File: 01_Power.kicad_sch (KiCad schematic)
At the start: 24 parts, among them Q1 SI3421DV, Q2 SI3421DV, U1 CYPD3177_24x

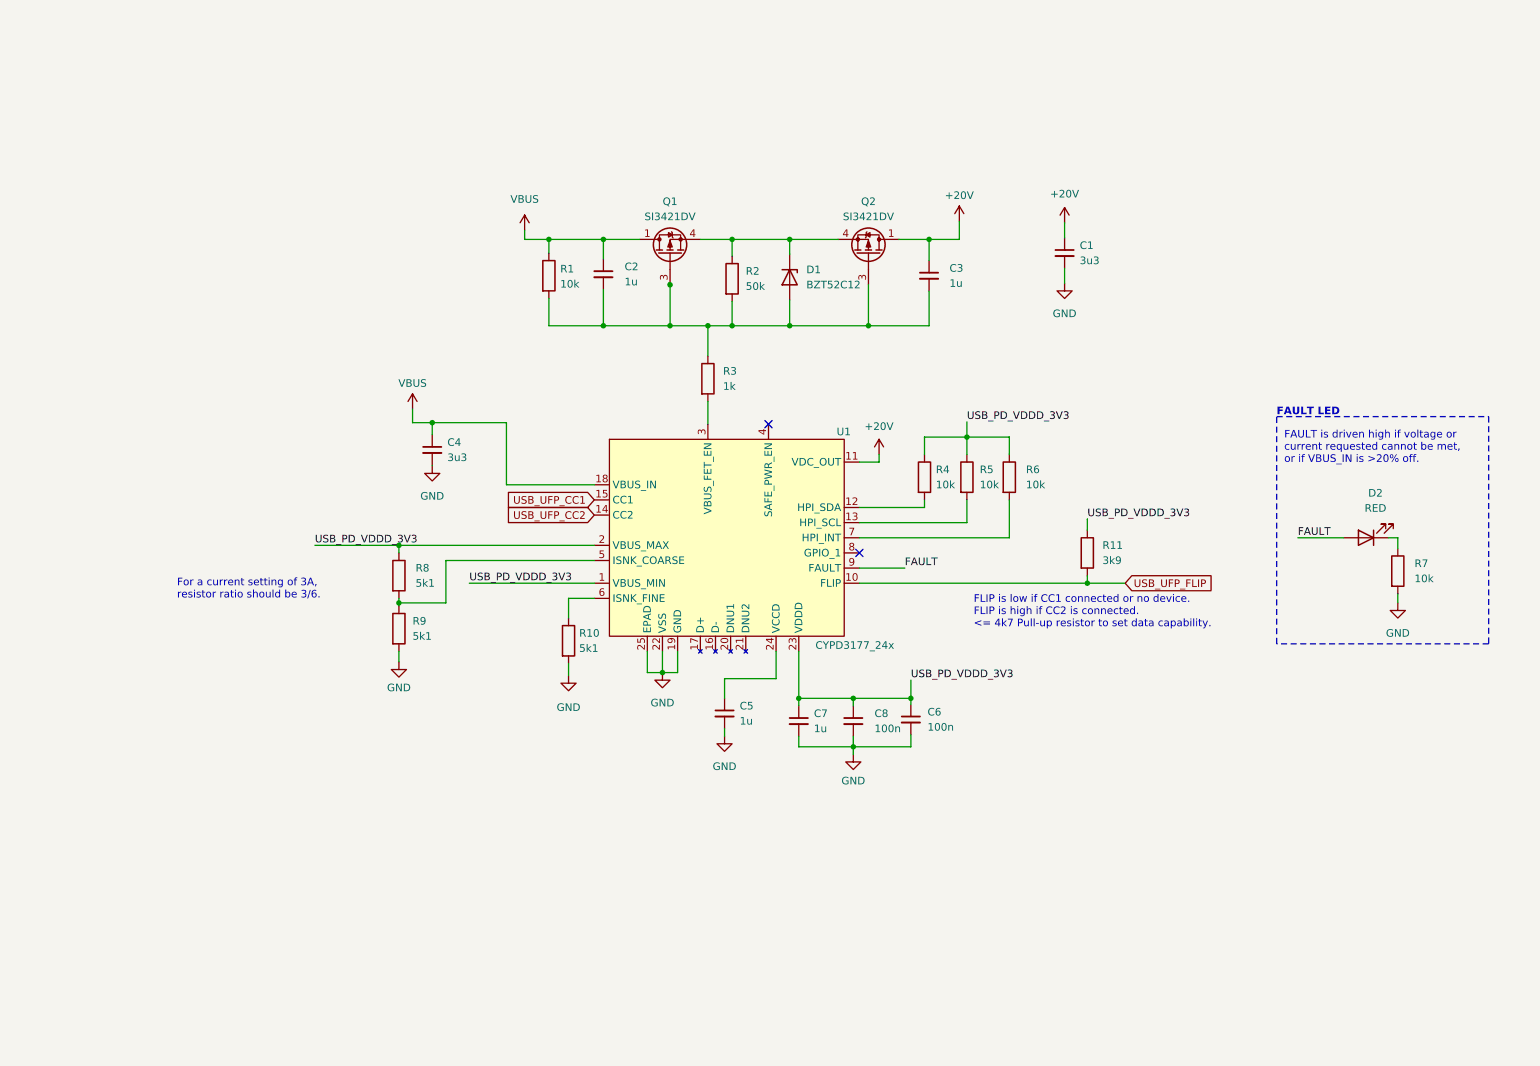
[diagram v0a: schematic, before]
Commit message: Add ESD protection for UFP, create buck converter model
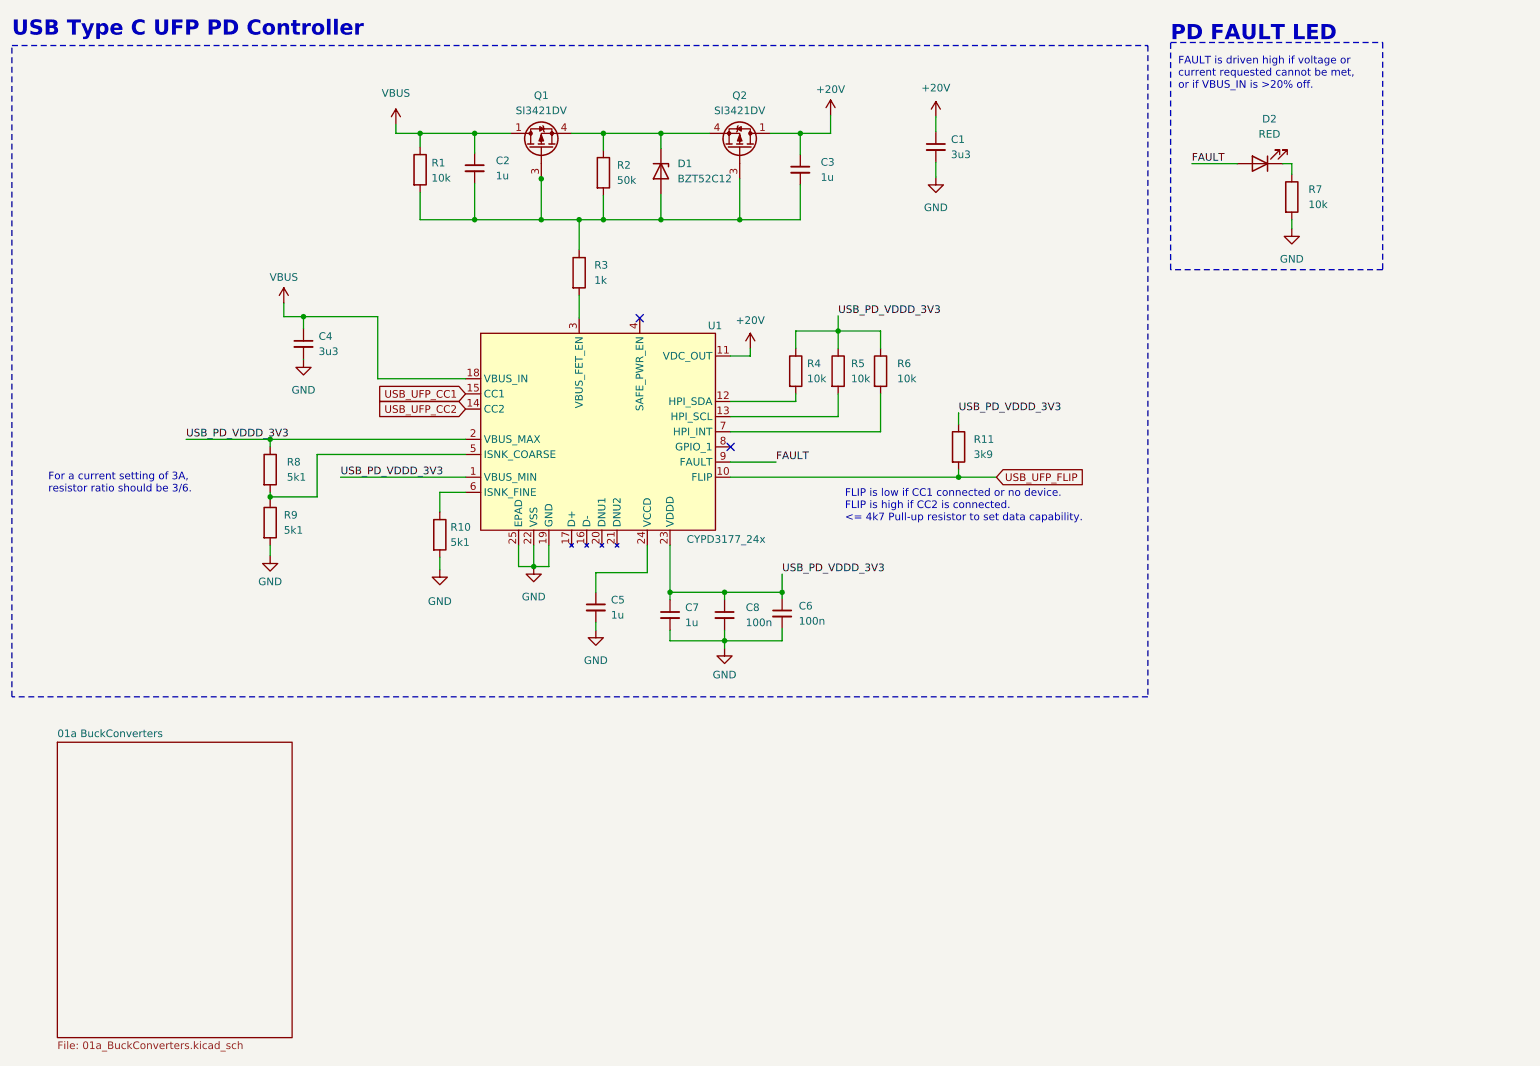
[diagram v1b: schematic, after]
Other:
- added sheet 01a BuckConverters (01a_BuckConverters.kicad_sch)
- note added: "PD FAULT LED"
- note added: "USB Type C UFP PD Controller"
- note removed: "FAULT LED"
- moved on the sheet: C1, C2, C3, C4, C5, C6, C7, C8, D1, D2, Q1, Q2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

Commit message: more work on the power section
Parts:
- C1: value 3u3 -> 100u
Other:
- sheet 01a BuckConverters renamed 01a VoltageRegulators
- added sheet 01b VoltageRegulators (01b_VoltageRegulators.kicad_sch)
- sheet 01a VoltageRegulators: file 01a_BuckConverters.kicad_sch -> 01a_VoltageRegulators.kicad_sch
- moved on the sheet: C1, C2, C3, C4, C5, C6, C7, C8, D1, D2, Q1, Q2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

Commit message: add usb hub controller schematic, fix up redriver
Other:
- removed sheet 01b VoltageRegulators
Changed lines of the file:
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@@
-    )
-  )
-  (sheet (at 67.31 137.16) (size 43.18 49.53) (fields_autoplaced)
-    (stroke (width 0.1524) (type solid))
-    (fill (color 0 0 0 0.0000))
-    (property "Sheetname" "01b VoltageRegulators" (at 67.31 136.4484 0)
-      (effects (font (size 1.27 1.27)) (justify left bottom))
-    )
-    (property "Sheetfile" "01b_VoltageRegulators.kicad_sch" (at 67.31 187.2746 0)
-      (effects (font (size 1.27 1.27)) (justify left top))
-    )
-    (instances
-      (project "USBHUB"
-        (path "/d5edc647-9ac3-4ac1-ab8a-57c77be3f4d3/2bd96af5-5a66-4797-badd-32cacbbf4fbd" (page "7"))
-      )
     )
   )

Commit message: finish up schematics and ERC
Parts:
- Q1, Q2: symbol catSink:SI3421DV -> CakeUSB:SI3421DV
- U1: symbol Cake_USB:CYPD3177_24x -> CakeUSB:CYPD3177_24x
- renumbered R9 to R10, R10 to R11, R7 to R3, R3 to R4, R4 to R5, R5 to R6, R6 to R7, R11 to R8, R8 to R9

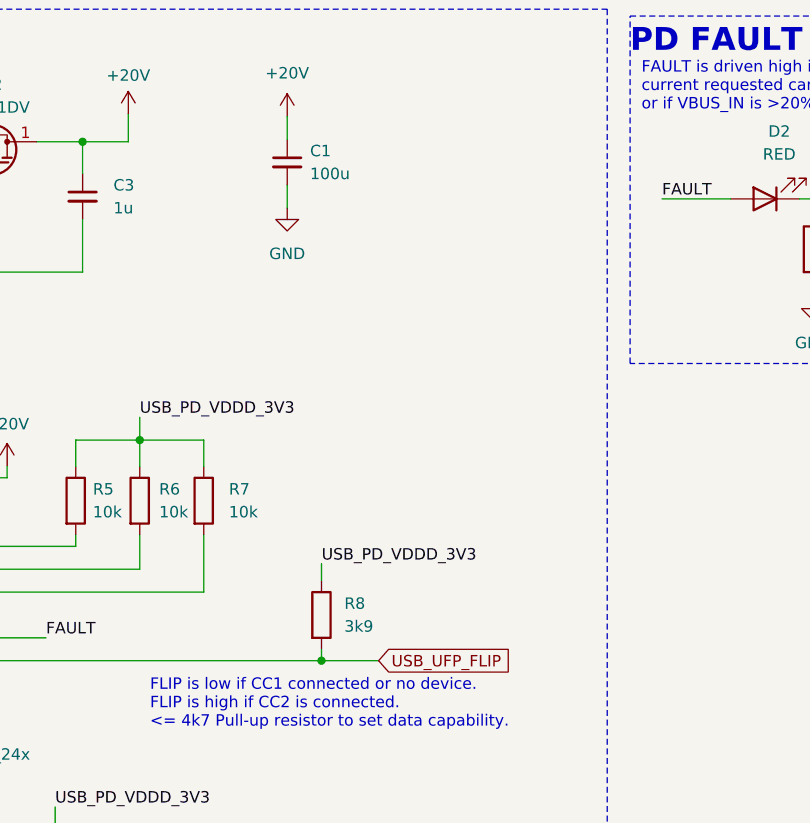
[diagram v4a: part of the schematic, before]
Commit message: finish setting footprints
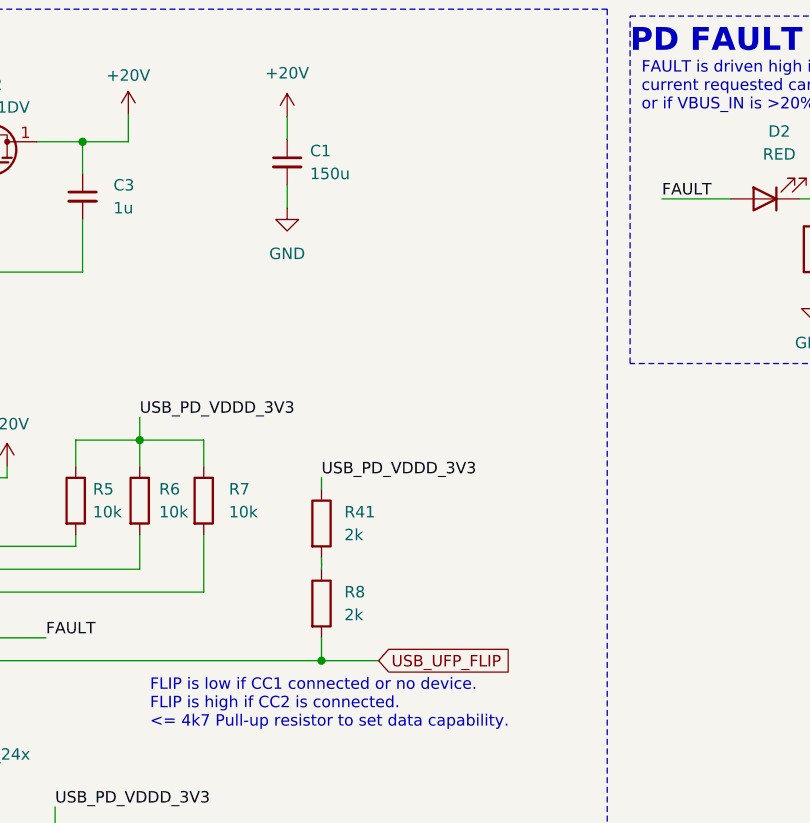
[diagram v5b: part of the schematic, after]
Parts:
- added R41: 2k, Resistor_SMD:R_0402_1005Metric, symbol Device:R
- C1: value 100u -> 150u; footprint Capacitor_SMD:C_0603_1608Metric -> Capacitor_SMD:C_Elec_6.3x7.7
- R8: value 3k9 -> 2k; footprint (none) -> Resistor_SMD:R_0402_1005Metric
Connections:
- net USB_PD_VDDD_3V3: now also R41.1; no longer R8.1
- new net: R41.2, R8.1
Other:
- moved on the sheet: R8
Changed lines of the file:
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@@
+    (stroke (width 0) (type default))
+  )
+  (wire (pts (xy 173.99 76.8879) (xy 173.99 76.2))
     (stroke (width 0) (type default))
   )
@@
     (stroke (width 0) (type default))
   )
-  (wire (pts (xy 173.99 86.36) (xy 173.99 87.63))
+  (wire (pts (xy 173.99 85.09) (xy 173.99 87.63))
     (stroke (width 0) (type default))
   )
@@
     (stroke (width 0) (type default))
   )
-  (wire (pts (xy 173.99 78.74) (xy 173.99 76.8879))
+  (wire (pts (xy 173.99 77.47) (xy 174.0084 76.8879))
     (stroke (width 0) (type default))
   )
@@
     (stroke (width 0) (type default))
   )
+  (wire (pts (xy 173.99 76.8879) (xy 174.0084 76.8879))
+    (stroke (width 0) (type default))
+  )
   (wire (pts (xy 153.797 63.119) (xy 153.797 66.04))
     (stroke (width 0) (type default))
@@
     (stroke (width 0) (type default))
   )
+  (wire (pts (xy 173.99 67.31) (xy 173.99 68.58))
+    (stroke (width 0) (type default))
+  )
   (wire (pts (xy 170.18 34.798) (xy 170.18 37.338))
     (stroke (width 0) (type default))
@@
   )
   (wire (pts (xy 125.603 106.934) (xy 125.603 108.204))
-    (stroke (width 0) (type default))
-  )
-  (wire (pts (xy 173.99 76.8879) (xy 174.0084 76.8879))
     (stroke (width 0) (type default))
   )
@@
     (effects (font (size 1.27 1.27)) (justify left bottom))
   )
-  (label "USB_PD_VDDD_3V3" (at 174.0084 76.8879 0) (fields_autoplaced)
+  (label "USB_PD_VDDD_3V3" (at 173.99 67.31 0) (fields_autoplaced)
     (effects (font (size 1.27 1.27)) (justify left bottom))
   )
@@
       (effects (font (size 1.27 1.27)) (justify left))
     )
-    (property "Value" "100u" (at 172.72 33.5343 0)
-      (effects (font (size 1.27 1.27)) (justify left))
-    )
-    (property "Footprint" "Capacitor_SMD:C_0603_1608Metric" (at 170.18 32.258 0)
+    (property "Value" "150u" (at 172.72 33.5343 0)
+      (effects (font (size 1.27 1.27)) (justify left))
+    )
+    (property "Footprint" "Capacitor_SMD:C_Elec_6.3x7.7" (at 170.18 32.258 0)
       (effects (font (size 1.27 1.27)) hide)
     )
@@
     )
   )
-  (symbol (lib_id "Device:R") (at 173.99 82.55 0) (unit 1)
-    (in_bom yes) (on_board yes) (dnp no) (fields_autoplaced)
-    (property "Reference" "R8" (at 176.53 81.28 0)
-      (effects (font (size 1.27 1.27)) (justify left))
-    )
-    (property "Value" "3k9" (at 176.53 83.82 0)
-      (effects (font (size 1.27 1.27)) (justify left))
-    )
-    (property "Footprint" "" (at 172.212 82.55 90)
-      (effects (font (size 1.27 1.27)) hide)
-    )
-    (property "Datasheet" "~" (at 173.99 82.55 0)
+  (symbol (lib_id "Device:R") (at 173.99 81.28 0) (unit 1)
+    (in_bom yes) (on_board yes) (dnp no) (fields_autoplaced)
+    (property "Reference" "R8" (at 176.53 80.01 0)
+      (effects (font (size 1.27 1.27)) (justify left))
+    )
+    (property "Value" "2k" (at 176.53 82.55 0)
+      (effects (font (size 1.27 1.27)) (justify left))
+    )
+    (property "Footprint" "Resistor_SMD:R_0402_1005Metric" (at 172.212 81.28 90)
+      (effects (font (size 1.27 1.27)) hide)
+    )
+    (property "Datasheet" "~" (at 173.99 81.28 0)
       (effects (font (size 1.27 1.27)) hide)
     )
@@
         )
       )
+    )
+  )
+  (symbol (lib_id "Device:R") (at 173.99 72.39 0) (unit 1)
+    (in_bom yes) (on_board yes) (dnp no) (fields_autoplaced)
+    (property "Reference" "R41" (at 176.53 71.12 0)
+      (effects (font (size 1.27 1.27)) (justify left))
+    )
+    (property "Value" "2k" (at 176.53 73.66 0)
+      (effects (font (size 1.27 1.27)) (justify left))
+    )
+    (property "Footprint" "Resistor_SMD:R_0402_1005Metric" (at 172.212 72.39 90)
+      (effects (font (size 1.27 1.27)) hide)
+    )
+    (property "Datasheet" "~" (at 173.99 72.39 0)
+      (effects (font (size 1.27 1.27)) hide)
+    )
+    (pin "2")
+    (pin "1")
+    (instances
+      (project "USBHUB"
+        (path "/d5edc647-9ac3-4ac1-ab8a-57c77be3f4d3/2bd96af5-5a66-4797-badd-32cacbbf4fbd"
+          (reference "R41") (unit 1)
+        )
+      )

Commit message: symbol fixes, switch ESD protection for USB datalines
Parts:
- U1: footprint Cake_USB:CYPD3177_24LQx_QFN-24_EP_4x4_Pitch0.5mm -> CakeUSB:CYPD3177_24LQx_QFN-24_EP_4x4_Pitch0.5mm
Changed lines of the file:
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@@
       (effects (font (size 1.27 1.27)) (justify left))
     )
-    (property "Footprint" "Cake_USB:CYPD3177_24LQx_QFN-24_EP_4x4_Pitch0.5mm" (at 161.163 46.99 0)
+    (property "Footprint" "CakeUSB:CYPD3177_24LQx_QFN-24_EP_4x4_Pitch0.5mm" (at 161.163 46.99 0)
       (effects (font (size 1.27 1.27)) hide)
     )

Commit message: fix symbols, route UFP DPs and voltage regs
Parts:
- R1, R3, R5, R6, R7: footprint Resistor_SMD:R_0603_1608Metric -> Resistor_SMD:R_0402_1005Metric
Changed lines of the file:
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@@
       (effects (font (size 1.27 1.27)) (justify left))
     )
-    (property "Footprint" "Resistor_SMD:R_0603_1608Metric" (at 152.019 69.85 90)
+    (property "Footprint" "Resistor_SMD:R_0402_1005Metric" (at 152.019 69.85 90)
       (effects (font (size 1.27 1.27)) hide)
     )
@@
       (effects (font (size 1.27 1.27)) (justify left))
     )
-    (property "Footprint" "Resistor_SMD:R_0603_1608Metric" (at 159.131 69.85 90)
+    (property "Footprint" "Resistor_SMD:R_0402_1005Metric" (at 159.131 69.85 90)
       (effects (font (size 1.27 1.27)) hide)
     )
@@
       (effects (font (size 1.27 1.27)) (justify left))
     )
-    (property "Footprint" "Resistor_SMD:R_0603_1608Metric" (at 81.915 36.068 90)
+    (property "Footprint" "Resistor_SMD:R_0402_1005Metric" (at 81.915 36.068 90)
       (effects (font (size 1.27 1.27)) hide)
     )
@@
       (effects (font (size 1.27 1.27)) (justify left))
     )
-    (property "Footprint" "Resistor_SMD:R_0603_1608Metric" (at 226.822 41.91 90)
+    (property "Footprint" "Resistor_SMD:R_0402_1005Metric" (at 226.822 41.91 90)
       (effects (font (size 1.27 1.27)) hide)
     )
@@
       (effects (font (size 1.27 1.27)) (justify left))
     )
-    (property "Footprint" "Resistor_SMD:R_0603_1608Metric" (at 144.907 69.85 90)
-      (effects (font (size 1.27 1.27)) hide)
-    )
+    (property "Footprint" "Resistor_SMD:R_0402_1005Metric" (at 144.907 69.85 90)
+      (effects (font (size 1.27 1.27)) hide)
+    )

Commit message: route power delivery controller
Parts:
- R1: footprint Resistor_SMD:R_0402_1005Metric -> Resistor_SMD:R_0603_1608Metric
- renumbered R9 to R10, R10 to R11, R11 to R12, R41 to R8, R8 to R9
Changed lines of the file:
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@@
   (symbol (lib_id "Device:R") (at 58.547 86.36 0) (unit 1)
     (in_bom yes) (on_board yes) (dnp no) (fields_autoplaced)
-    (property "Reference" "R9" (at 61.341 85.09 0)
+    (property "Reference" "R10" (at 61.341 85.09 0)
       (effects (font (size 1.27 1.27)) (justify left))
     )
@@
       (project "USBHUB"
         (path "/d5edc647-9ac3-4ac1-ab8a-57c77be3f4d3/2bd96af5-5a66-4797-badd-32cacbbf4fbd"
-          (reference "R9") (unit 1)
+          (reference "R10") (unit 1)
         )
       )
@@
       (effects (font (size 1.27 1.27)) (justify left))
     )
-    (property "Footprint" "Resistor_SMD:R_0402_1005Metric" (at 81.915 36.068 90)
+    (property "Footprint" "Resistor_SMD:R_0603_1608Metric" (at 81.915 36.068 90)
       (effects (font (size 1.27 1.27)) hide)
     )
@@
   (symbol (lib_id "Device:R") (at 173.99 81.28 0) (unit 1)
     (in_bom yes) (on_board yes) (dnp no) (fields_autoplaced)
-    (property "Reference" "R8" (at 176.53 80.01 0)
+    (property "Reference" "R9" (at 176.53 80.01 0)
       (effects (font (size 1.27 1.27)) (justify left))
     )
@@
       (project "USBHUB"
         (path "/d5edc647-9ac3-4ac1-ab8a-57c77be3f4d3/2bd96af5-5a66-4797-badd-32cacbbf4fbd"
-          (reference "R8") (unit 1)
+          (reference "R9") (unit 1)
         )
       )
@@
   (symbol (lib_id "Device:R") (at 173.99 72.39 0) (unit 1)
     (in_bom yes) (on_board yes) (dnp no) (fields_autoplaced)
-    (property "Reference" "R41" (at 176.53 71.12 0)
+    (property "Reference" "R8" (at 176.53 71.12 0)
       (effects (font (size 1.27 1.27)) (justify left))
     )
@@
       (project "USBHUB"
         (path "/d5edc647-9ac3-4ac1-ab8a-57c77be3f4d3/2bd96af5-5a66-4797-badd-32cacbbf4fbd"
-          (reference "R41") (unit 1)
+          (reference "R8") (unit 1)
         )
       )
@@
   (symbol (lib_id "Device:R") (at 58.547 95.25 0) (unit 1)
     (in_bom yes) (on_board yes) (dnp no) (fields_autoplaced)
-    (property "Reference" "R10" (at 60.833 93.98 0)
+    (property "Reference" "R11" (at 60.833 93.98 0)
       (effects (font (size 1.27 1.27)) (justify left))
     )
@@
       (project "USBHUB"
         (path "/d5edc647-9ac3-4ac1-ab8a-57c77be3f4d3/2bd96af5-5a66-4797-badd-32cacbbf4fbd"
-          (reference "R10") (unit 1)
+          (reference "R11") (unit 1)
         )
       )
@@
   (symbol (lib_id "Device:R") (at 86.995 97.282 0) (unit 1)
     (in_bom yes) (on_board yes) (dnp no) (fields_autoplaced)
-    (property "Reference" "R11" (at 88.773 96.012 0)
+    (property "Reference" "R12" (at 88.773 96.012 0)
       (effects (font (size 1.27 1.27)) (justify left))
     )
@@
       (project "USBHUB"
         (path "/d5edc647-9ac3-4ac1-ab8a-57c77be3f4d3/2bd96af5-5a66-4797-badd-32cacbbf4fbd"
-          (reference "R11") (unit 1)
-        )
-      )
+          (reference "R12") (unit 1)
+        )
+      )
